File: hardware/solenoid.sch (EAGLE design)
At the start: 40 parts, among them U2 AP2204R

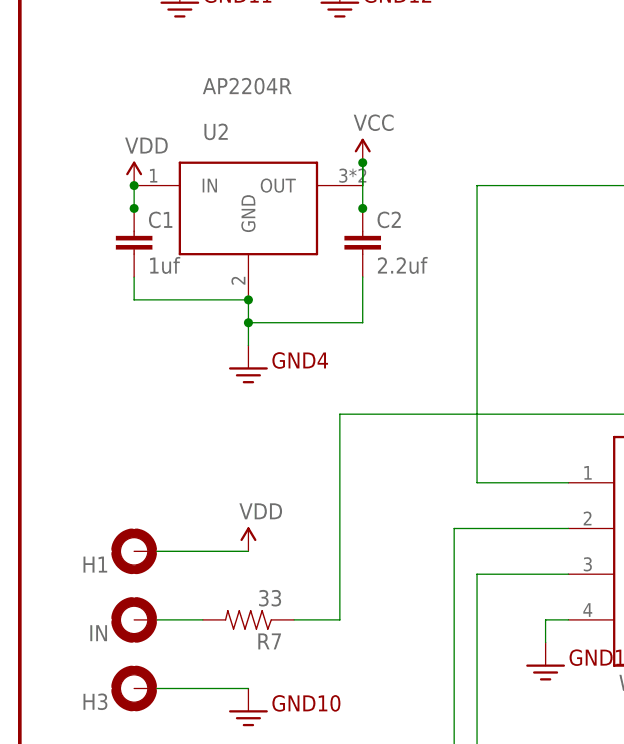
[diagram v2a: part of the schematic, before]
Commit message: Fixed problem with reguslator having wrong footprint.
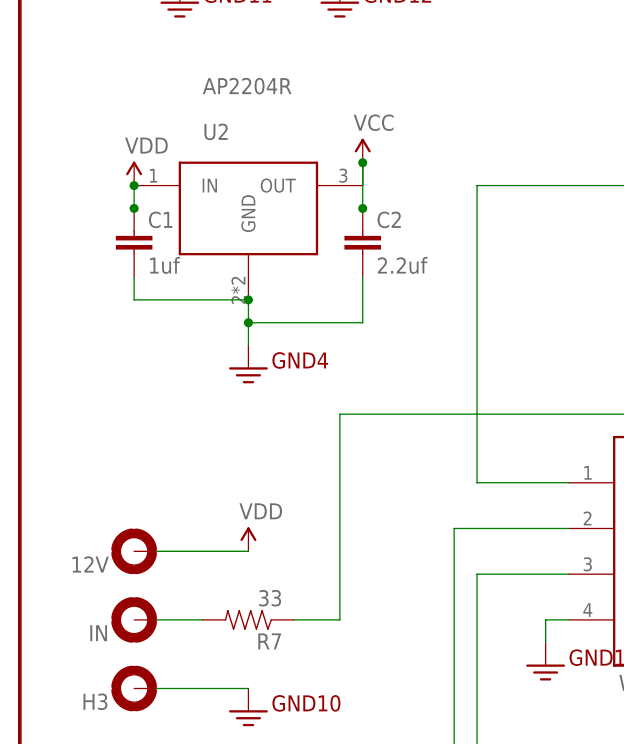
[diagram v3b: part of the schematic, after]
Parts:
- FRAME1: CREVISON 1.0 -> 1.1
- renumbered H1 to 12V
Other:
- moved on the sheet: U2
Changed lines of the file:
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@@
 <?xml version="1.0" encoding="utf-8"?>
 <!DOCTYPE eagle SYSTEM "eagle.dtd">
-<eagle version="8.2.0">
+<eagle version="8.2.1">
 <drawing>
 <settings>
@@
 <part name="D3" library="mishafarms" deviceset="SUPPRESSOR-" device="SMBJ" value="36V"/>
 <part name="OUT-B" library="holes" deviceset="MOUNT-PAD-ROUND" device="2.8"/>
-<part name="H1" library="holes" deviceset="MOUNT-PAD-ROUND" device="2.8"/>
+<part name="12V" library="holes" deviceset="MOUNT-PAD-ROUND" device="2.8"/>
 <part name="IN" library="holes" deviceset="MOUNT-PAD-ROUND" device="2.8"/>
 <part name="H3" library="holes" deviceset="MOUNT-PAD-ROUND" device="2.8"/>
@@
 <part name="H6" library="holes" deviceset="MOUNT-PAD-ROUND" device="2.8"/>
 <part name="FRAME1" library="SparkFun-Aesthetics" deviceset="FRAME-LETTER" device="NO_PACKAGE">
-<attribute name="CREVISON" value="1.0"/>
+<attribute name="CREVISON" value="1.1"/>
 <attribute name="DESIGNER" value="Michael L. Weiss"/>
 <attribute name="VERSION" value="v1.0"/>
@@
 <attribute name="NAME" x="165.354" y="79.3242" size="1.778" layer="95"/>
 </instance>
-<instance part="H1" gate="G$1" x="12.7" y="101.6" smashed="yes" rot="R180">
+<instance part="12V" gate="G$1" x="12.7" y="101.6" smashed="yes" rot="R180">
 <attribute name="NAME" x="9.906" y="101.0158" size="1.778" layer="95" rot="R180"/>
 </instance>
@@
 <pinref part="SUPPLY13" gate="VDD" pin="VDD"/>
 <wire x1="25.4" y1="101.6" x2="15.24" y2="101.6" width="0.1524" layer="91"/>
-<pinref part="H1" gate="G$1" pin="MOUNT"/>
-</segment>
-<segment>
+<pinref part="12V" gate="G$1" pin="MOUNT"/>
+</segment>
+<segment>

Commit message: Changed from 470nf to 1uf for the filter cap now I get no chatter on my solenoids when I have the level at 127.
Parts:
- C3, C4, C7: value 400nf -> 1uf
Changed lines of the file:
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@@
 <part name="SUPPLY3" library="SparkFun-Aesthetics" deviceset="VCC" device=""/>
 <part name="R" library="led" deviceset="LED" device="CHIPLED_0805"/>
-<part name="C3" library="SparkFun-Capacitors" deviceset="CAP" device="0805" value="400nf"/>
+<part name="C3" library="SparkFun-Capacitors" deviceset="CAP" device="0805" value="1uf"/>
 <part name="GND5" library="SparkFun-Aesthetics" deviceset="GND2" device=""/>
 <part name="D2" library="mishafarms" deviceset="SUPPRESSOR-" device="SMBJ" value="36V"/>
@@
 <part name="SUPPLY9" library="SparkFun-Aesthetics" deviceset="VCC" device=""/>
 <part name="G" library="led" deviceset="LED" device="CHIPLED_0805"/>
-<part name="C7" library="SparkFun-Capacitors" deviceset="CAP" device="0805" value="400nf"/>
+<part name="C7" library="SparkFun-Capacitors" deviceset="CAP" device="0805" value="1uf"/>
 <part name="GND15" library="SparkFun-Aesthetics" deviceset="GND2" device=""/>
 <part name="D4" library="mishafarms" deviceset="SUPPRESSOR-" device="SMBJ" value="36V"/>
@@
 <part name="SUPPLY7" library="SparkFun-Aesthetics" deviceset="VCC" device=""/>
 <part name="B" library="led" deviceset="LED" device="CHIPLED_0805"/>
-<part name="C4" library="SparkFun-Capacitors" deviceset="CAP" device="0805" value="400nf"/>
+<part name="C4" library="SparkFun-Capacitors" deviceset="CAP" device="0805" value="1uf"/>
 <part name="GND8" library="SparkFun-Aesthetics" deviceset="GND2" device=""/>
 <part name="D3" library="mishafarms" deviceset="SUPPRESSOR-" device="SMBJ" value="36V"/>
